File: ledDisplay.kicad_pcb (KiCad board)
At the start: 2 copper layers, 50 x 50 mm, 63 parts, among them J1 BAT, P1 USB_C_Receptacle_USB2.0_14P, SW1 BUTTON, U1 MCP73833-xxx-UN, U2 LD1117S33TR_SOT223, U3 W25Q128JVS, U4 RP2040, Y1 12MHz

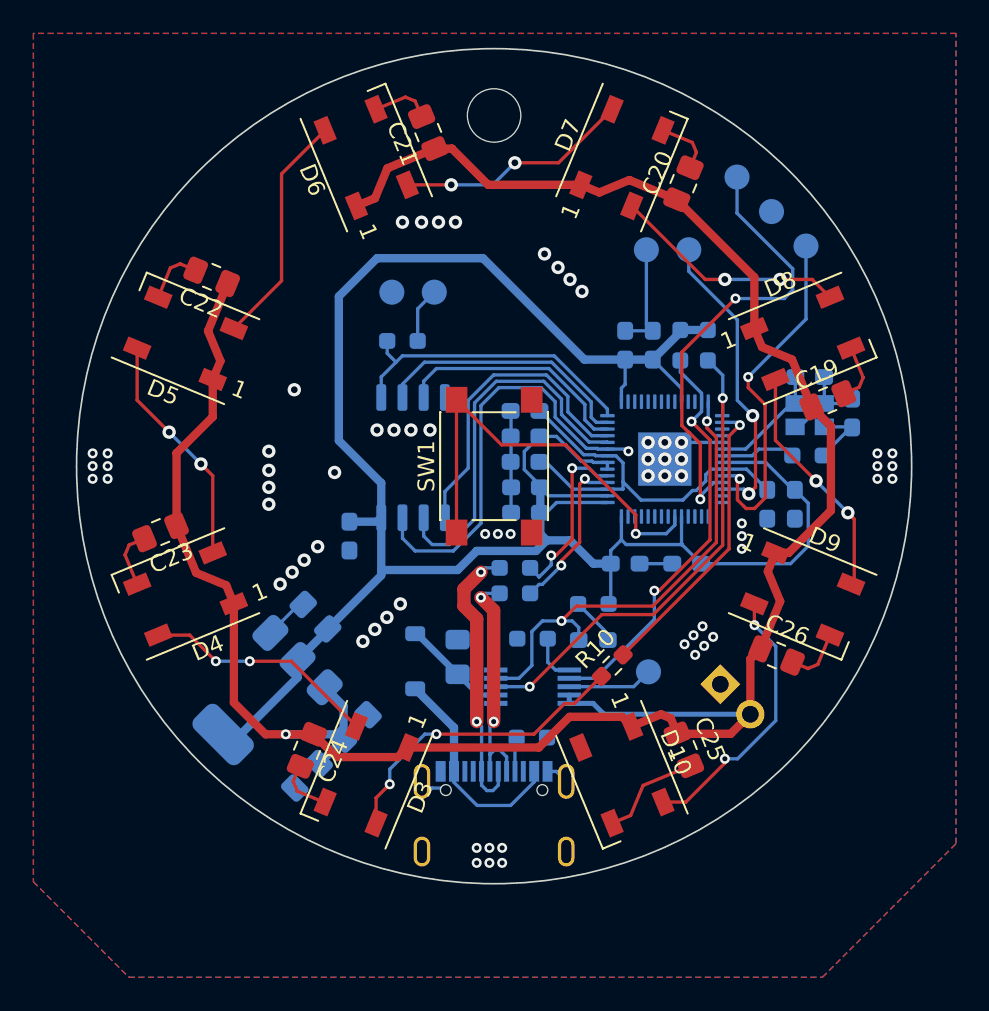
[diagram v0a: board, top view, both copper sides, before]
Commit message: change PCB descriptions
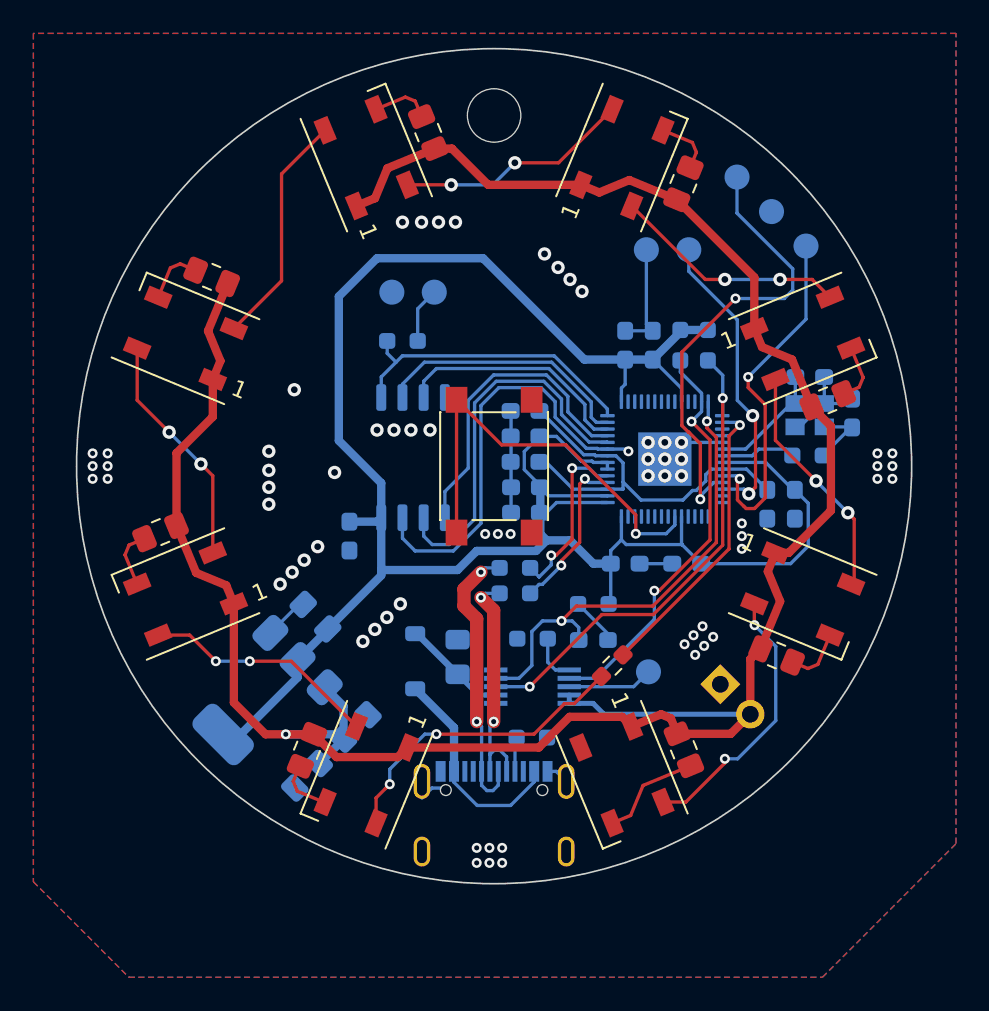
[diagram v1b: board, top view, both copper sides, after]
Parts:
- R3: value 1k -> 5.1k
- renumbered SW1 to SWe
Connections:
- C12 pad 1: VBUS -> Net-(C12-Pad1)
- P1 pad A4: Net-(D1-A) -> Net-(C12-Pad1)
- P1 pad A9: Net-(D1-A) -> Net-(C12-Pad1)
- P1 pad B4: Net-(D1-A) -> Net-(C12-Pad1)
- P1 pad B9: Net-(D1-A) -> Net-(C12-Pad1)
- U1 pad 1: VBUS -> Net-(C12-Pad1)
- U1 pad 2: VBUS -> Net-(C12-Pad1)
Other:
- board text added: "BOOT"
- board text added: "RST"
- board text removed: "Li-Po 3.7V Battery"

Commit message: update pcb
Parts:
- removed D1: 1N4148W, Diode_SMD:D_SOD-123
- removed TP1: TestPoint, TestPoint:TestPoint_Pad_D1.5mm
- moved C12 1.66 mm to (170.7, 100.1)
- renumbered SWe to SW1
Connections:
- C12 pad 1: Net-(C12-Pad1) -> /THERM
- P1 pad A4: Net-(C12-Pad1) -> /THERM
- P1 pad A9: Net-(C12-Pad1) -> /THERM
- P1 pad B4: Net-(C12-Pad1) -> /THERM
- P1 pad B9: Net-(C12-Pad1) -> /THERM
- U1 pad 1: Net-(C12-Pad1) -> /THERM
- U1 pad 2: Net-(C12-Pad1) -> /THERM
- U1 pad 8: Net-(U1-THERM) -> /THERM
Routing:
- net /THERM: track 0.00 -> 19.2 mm
- net Net-(D1-A): track 13.2 -> 0.00 mm
- net VBUS: track 6.85 -> 0.00 mm
- net Net-(U1-THERM): track 5.11 -> 0.00 mm
